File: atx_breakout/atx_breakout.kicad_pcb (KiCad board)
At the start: 2 copper layers, 1 part, among them J1 ATX-24

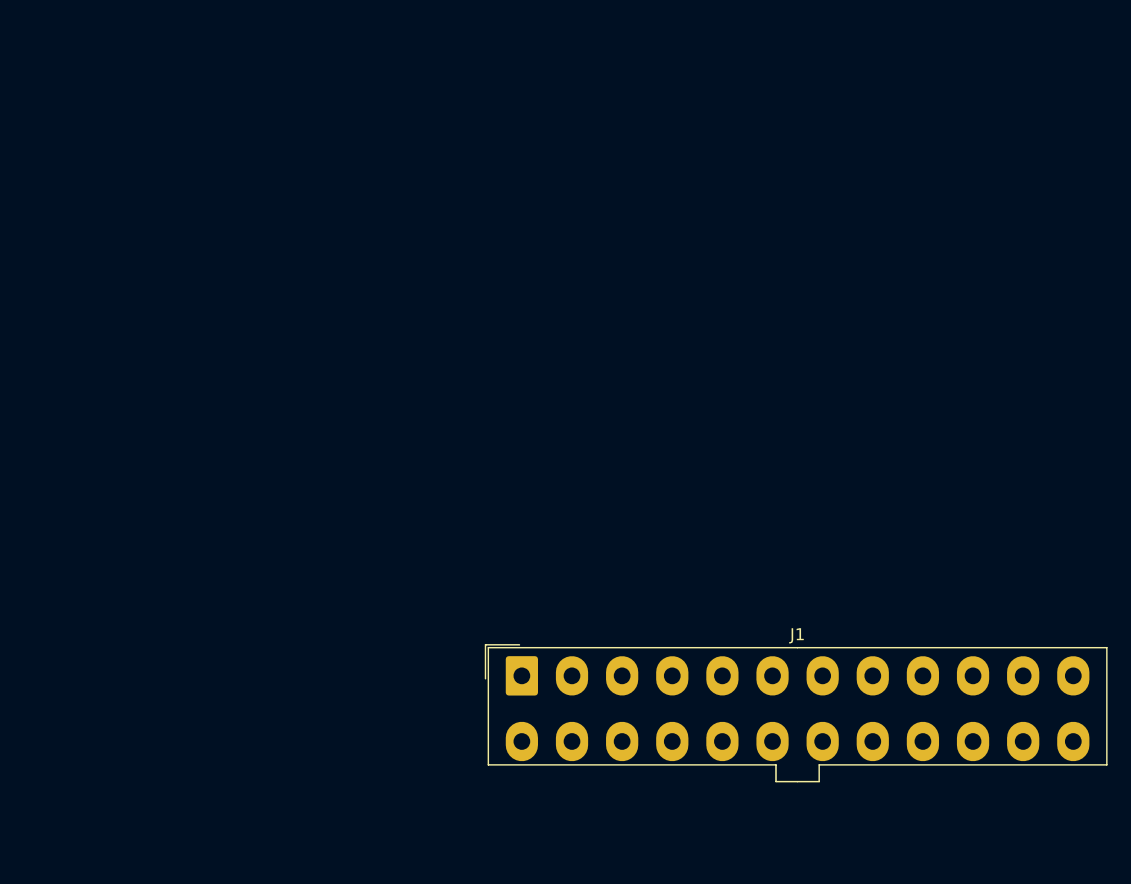
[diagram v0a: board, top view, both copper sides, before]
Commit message: Progress on atx breakout
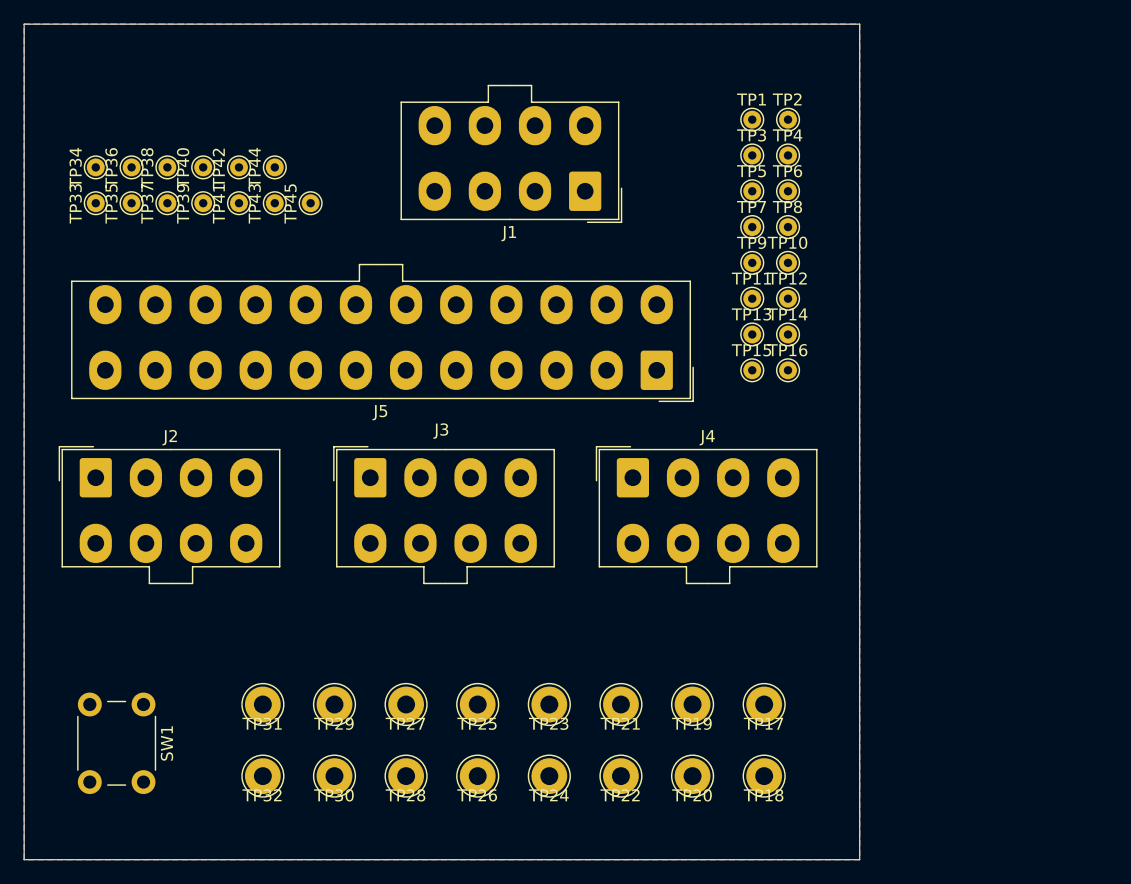
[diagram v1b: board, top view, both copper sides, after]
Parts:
- added J2: Conn_02x04_Top_Bottom, Connector_Molex:Molex_Mini-Fit_Jr_5566-08A_2x04_P4.20mm_Vertical, F.Cu at (6.00, 38.0)
- added J3: Conn_02x04_Top_Bottom, Connector_Molex:Molex_Mini-Fit_Jr_5566-08A_2x04_P4.20mm_Vertical, F.Cu at (29.0, 38.0)
- added J4: Conn_02x04_Top_Bottom, Connector_Molex:Molex_Mini-Fit_Jr_5566-08A_2x04_P4.20mm_Vertical, F.Cu at (51.0, 38.0)
- added J5: ATX-24, Connector_Molex:Molex_Mini-Fit_Jr_5566-24A_2x12_P4.20mm_Vertical, F.Cu at (53.0, 29.0)
- added SW1: SW_SPST, Button_Switch_THT:SW_PUSH_6mm, F.Cu at (10.0, 57.0)
- added TP1: TestPoint, TestPoint:TestPoint_THTPad_D1.5mm_Drill0.7mm, F.Cu at (61.0, 8.00)
- added TP10: TestPoint, TestPoint:TestPoint_THTPad_D1.5mm_Drill0.7mm, F.Cu at (64.0, 20.0)
- added TP11: TestPoint, TestPoint:TestPoint_THTPad_D1.5mm_Drill0.7mm, F.Cu at (61.0, 23.0)
- added TP12: TestPoint, TestPoint:TestPoint_THTPad_D1.5mm_Drill0.7mm, F.Cu at (64.0, 23.0)
- added TP13: TestPoint, TestPoint:TestPoint_THTPad_D1.5mm_Drill0.7mm, F.Cu at (61.0, 26.0)
- added TP14: TestPoint, TestPoint:TestPoint_THTPad_D1.5mm_Drill0.7mm, F.Cu at (64.0, 26.0)
- added TP15: TestPoint, TestPoint:TestPoint_THTPad_D1.5mm_Drill0.7mm, F.Cu at (61.0, 29.0)
- added TP16: TestPoint, TestPoint:TestPoint_THTPad_D1.5mm_Drill0.7mm, F.Cu at (64.0, 29.0)
- added TP17: TestPoint, TestPoint:TestPoint_THTPad_D3.0mm_Drill1.5mm, F.Cu at (62.0, 57.0)
- added TP18: TestPoint, TestPoint:TestPoint_THTPad_D3.0mm_Drill1.5mm, F.Cu at (62.0, 63.0)
- added TP19: TestPoint, TestPoint:TestPoint_THTPad_D3.0mm_Drill1.5mm, F.Cu at (56.0, 57.0)
- added TP2: TestPoint, TestPoint:TestPoint_THTPad_D1.5mm_Drill0.7mm, F.Cu at (64.0, 8.00)
- added TP20: TestPoint, TestPoint:TestPoint_THTPad_D3.0mm_Drill1.5mm, F.Cu at (56.0, 63.0)
- added TP21: TestPoint, TestPoint:TestPoint_THTPad_D3.0mm_Drill1.5mm, F.Cu at (50.0, 57.0)
- added TP22: TestPoint, TestPoint:TestPoint_THTPad_D3.0mm_Drill1.5mm, F.Cu at (50.0, 63.0)
- added TP23: TestPoint, TestPoint:TestPoint_THTPad_D3.0mm_Drill1.5mm, F.Cu at (44.0, 57.0)
- added TP24: TestPoint, TestPoint:TestPoint_THTPad_D3.0mm_Drill1.5mm, F.Cu at (44.0, 63.0)
- added TP25: TestPoint, TestPoint:TestPoint_THTPad_D3.0mm_Drill1.5mm, F.Cu at (38.0, 57.0)
- added TP26: TestPoint, TestPoint:TestPoint_THTPad_D3.0mm_Drill1.5mm, F.Cu at (38.0, 63.0)
- added TP27: TestPoint, TestPoint:TestPoint_THTPad_D3.0mm_Drill1.5mm, F.Cu at (32.0, 57.0)
- added TP28: TestPoint, TestPoint:TestPoint_THTPad_D3.0mm_Drill1.5mm, F.Cu at (32.0, 63.0)
- added TP29: TestPoint, TestPoint:TestPoint_THTPad_D3.0mm_Drill1.5mm, F.Cu at (26.0, 57.0)
- added TP3: TestPoint, TestPoint:TestPoint_THTPad_D1.5mm_Drill0.7mm, F.Cu at (61.0, 11.0)
- added TP30: TestPoint, TestPoint:TestPoint_THTPad_D3.0mm_Drill1.5mm, F.Cu at (26.0, 63.0)
- added TP31: TestPoint, TestPoint:TestPoint_THTPad_D3.0mm_Drill1.5mm, F.Cu at (20.0, 57.0)
- added TP32: TestPoint, TestPoint:TestPoint_THTPad_D3.0mm_Drill1.5mm, F.Cu at (20.0, 63.0)
- added TP33: TestPoint, TestPoint:TestPoint_THTPad_D1.5mm_Drill0.7mm, F.Cu at (6.00, 15.0)
- added TP34: TestPoint, TestPoint:TestPoint_THTPad_D1.5mm_Drill0.7mm, F.Cu at (6.00, 12.0)
- added TP35: TestPoint, TestPoint:TestPoint_THTPad_D1.5mm_Drill0.7mm, F.Cu at (9.00, 15.0)
- added TP36: TestPoint, TestPoint:TestPoint_THTPad_D1.5mm_Drill0.7mm, F.Cu at (9.00, 12.0)
- added TP37: TestPoint, TestPoint:TestPoint_THTPad_D1.5mm_Drill0.7mm, F.Cu at (12.0, 15.0)
- added TP38: TestPoint, TestPoint:TestPoint_THTPad_D1.5mm_Drill0.7mm, F.Cu at (12.0, 12.0)
- added TP39: TestPoint, TestPoint:TestPoint_THTPad_D1.5mm_Drill0.7mm, F.Cu at (15.0, 15.0)
- added TP4: TestPoint, TestPoint:TestPoint_THTPad_D1.5mm_Drill0.7mm, F.Cu at (64.0, 11.0)
- added TP40: TestPoint, TestPoint:TestPoint_THTPad_D1.5mm_Drill0.7mm, F.Cu at (15.0, 12.0)
- added TP41: TestPoint, TestPoint:TestPoint_THTPad_D1.5mm_Drill0.7mm, F.Cu at (18.0, 15.0)
- added TP42: TestPoint, TestPoint:TestPoint_THTPad_D1.5mm_Drill0.7mm, F.Cu at (18.0, 12.0)
- added TP43: TestPoint, TestPoint:TestPoint_THTPad_D1.5mm_Drill0.7mm, F.Cu at (21.0, 15.0)
- added TP44: TestPoint, TestPoint:TestPoint_THTPad_D1.5mm_Drill0.7mm, F.Cu at (21.0, 12.0)
- added TP45: TestPoint, TestPoint:TestPoint_THTPad_D1.5mm_Drill0.7mm, F.Cu at (24.0, 15.0)
- added TP5: TestPoint, TestPoint:TestPoint_THTPad_D1.5mm_Drill0.7mm, F.Cu at (61.0, 14.0)
- added TP6: TestPoint, TestPoint:TestPoint_THTPad_D1.5mm_Drill0.7mm, F.Cu at (64.0, 14.0)
- added TP7: TestPoint, TestPoint:TestPoint_THTPad_D1.5mm_Drill0.7mm, F.Cu at (61.0, 17.0)
- added TP8: TestPoint, TestPoint:TestPoint_THTPad_D1.5mm_Drill0.7mm, F.Cu at (64.0, 17.0)
- added TP9: TestPoint, TestPoint:TestPoint_THTPad_D1.5mm_Drill0.7mm, F.Cu at (61.0, 20.0)
- J1: value ATX-24 -> Conn_02x04_Top_Bottom; footprint Connector_Molex:Molex_Mini-Fit_Jr_5566-24A_2x12_P4.20mm_Vertical -> Connector_Molex:Molex_Mini-Fit_Jr_5566-08A_2x04_P4.20mm_Vertical
- moved J1 40.9 mm to (47.0, 14.0), turned to 180 degrees
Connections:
- J1 pad 1: Net-(J1-+3.3V-Pad1) -> GND
- J1 pad 2: Net-(J1-+3.3V-Pad1) -> GND
- J1 pad 3: Net-(J1-GND-Pad15) -> GND
- J1 pad 4: Net-(J1-+5V-Pad21) -> GND
- J1 pad 5: Net-(J1-GND-Pad15) -> +12V
- J1 pad 6: Net-(J1-+5V-Pad21) -> +12V
- J1 pad 7: Net-(J1-GND-Pad15) -> +12V
- J1 pad 8: unconnected-(J1-PWR_OK-Pad8) -> +12V
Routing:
- added copper zone on F.Cu, net +12V
- added copper zone on B.Cu, net GND
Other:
- board outline added: 70 x 70 mm
- rule pad_to_mask_clearance: 0 -> 0.038

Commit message: Progress on atx breakout
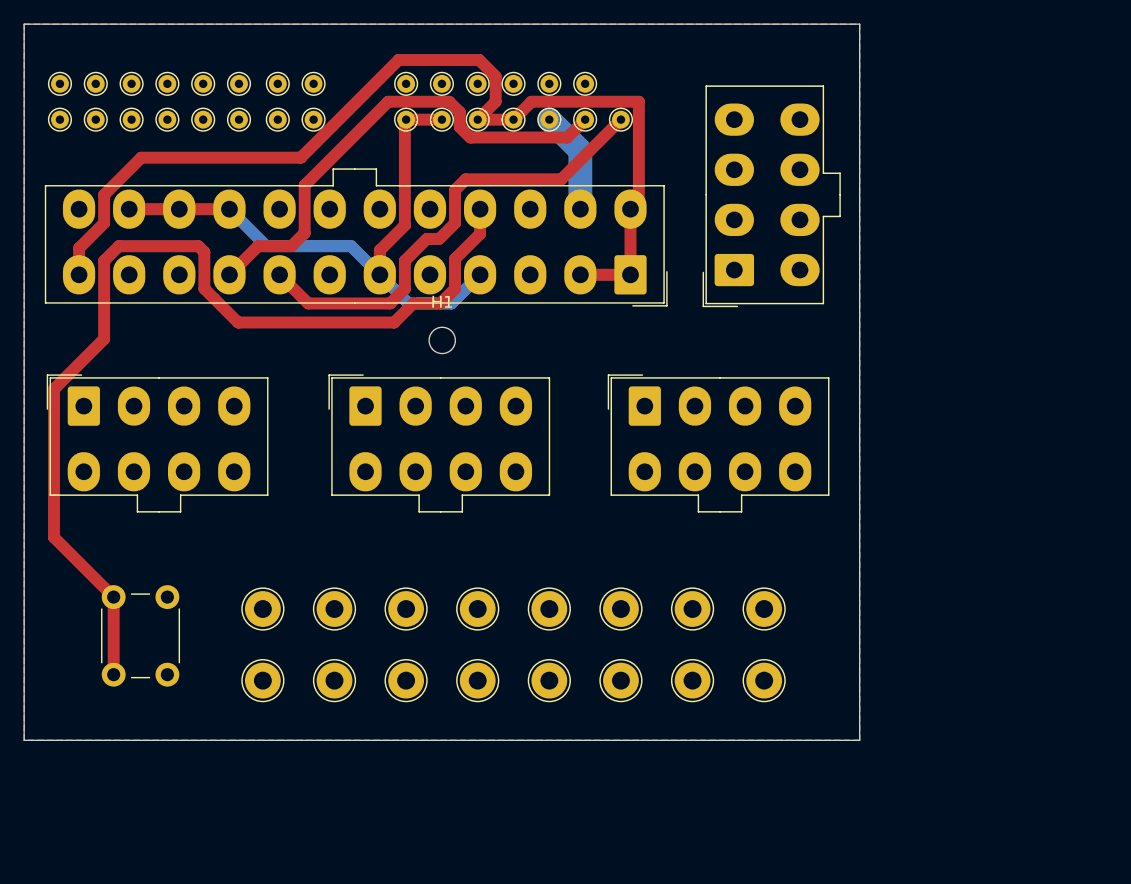
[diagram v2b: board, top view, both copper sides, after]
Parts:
- added H1: MountingHole, MountingHole:MountingHole_2.2mm_M2, F.Cu at (35.0, 26.5)
- moved TP2 61.1 mm to (3.00, 5.00), turned to 90 degrees
- moved TP4 58.3 mm to (6.00, 5.00), turned to 90 degrees
- moved TP1 58.0 mm to (3.00, 8.00), turned to 90 degrees
- moved TP6 55.7 mm to (9.00, 5.00), turned to 90 degrees
- moved TP3 55.1 mm to (6.00, 8.00), turned to 90 degrees
- moved TP8 53.4 mm to (12.0, 5.00), turned to 90 degrees
- moved TP5 52.3 mm to (9.00, 8.00), turned to 90 degrees
- moved TP10 51.2 mm to (15.0, 5.00), turned to 90 degrees
- moved TP7 49.8 mm to (12.0, 8.00), turned to 90 degrees
- moved TP12 49.4 mm to (18.0, 5.00), turned to 90 degrees
- moved TP14 47.6 mm to (21.2, 5.00), turned to 90 degrees
- moved TP9 47.5 mm to (15.0, 8.00), turned to 90 degrees
- moved TP16 46.4 mm to (24.2, 5.00), turned to 90 degrees
- moved TP11 45.5 mm to (18.0, 8.00), turned to 90 degrees
- moved TP13 43.6 mm to (21.2, 8.00), turned to 90 degrees
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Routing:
- net +3.3V: track 0.00 -> 83.0 mm
- net Net-(J5-PS_ON#): track 0.00 -> 81.6 mm
- net +5V: track 0.00 -> 50.6 mm
- net VBUS: track 0.00 -> 40.7 mm
- net /PWR_OK: track 0.00 -> 39.0 mm
- net -12V: track 0.00 -> 8.58 mm
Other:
- board size 70 x 70 mm -> 70 x 60 mm

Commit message: Finished atx breakout
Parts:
- removed SW1: SW_SPST, Button_Switch_THT:SW_PUSH_6mm
- added U1: SW_DPDT_PS-70N, misc:SW_DPDT_PS-70N, F.Cu at (9.00, 51.0)
- J1, J2, J3, J4: footprint Connector_Molex:Molex_Mini-Fit_Jr_5566-08A_2x04_P4.20mm_Vertical -> misc:Molex_Mini-Fit_Jr_5566-08A_2x04_P4.20mm_XY_Vertical
- J5: footprint Connector_Molex:Molex_Mini-Fit_Jr_5566-24A_2x12_P4.20mm_Vertical -> misc:Molex_Mini-Fit_Jr_5566-24A_2x12_P4.20mm_XY_Vertical
- moved J3 1.17 mm to (28.0, 33.0)
- moved J2 1.00 mm to (5.00, 33.0)
- moved J4 1.00 mm to (52.0, 33.0)
- moved J1 0.78 mm to (59.0, 20.0)
- moved H1 0.50 mm to (35.0, 27.0)
- moved TP13 0.25 mm to (21.0, 8.00)
- moved TP14 0.25 mm to (21.0, 5.00)
- moved TP15 0.25 mm to (24.0, 8.00)
- moved TP16 0.25 mm to (24.0, 5.00)
- moved J5 0.20 mm to (51.0, 21.0)
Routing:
- net Net-(J5-PS_ON#): track 81.6 -> 64.4 mm
- net /PWR_OK: track 39.0 -> 55.5 mm
- net +3.3V: track 83.0 -> 67.1 mm
- net VBUS: track 40.7 -> 56.1 mm
- net +5V: track 50.6 -> 56.2 mm
- net -12V: track 8.58 -> 9.96 mm

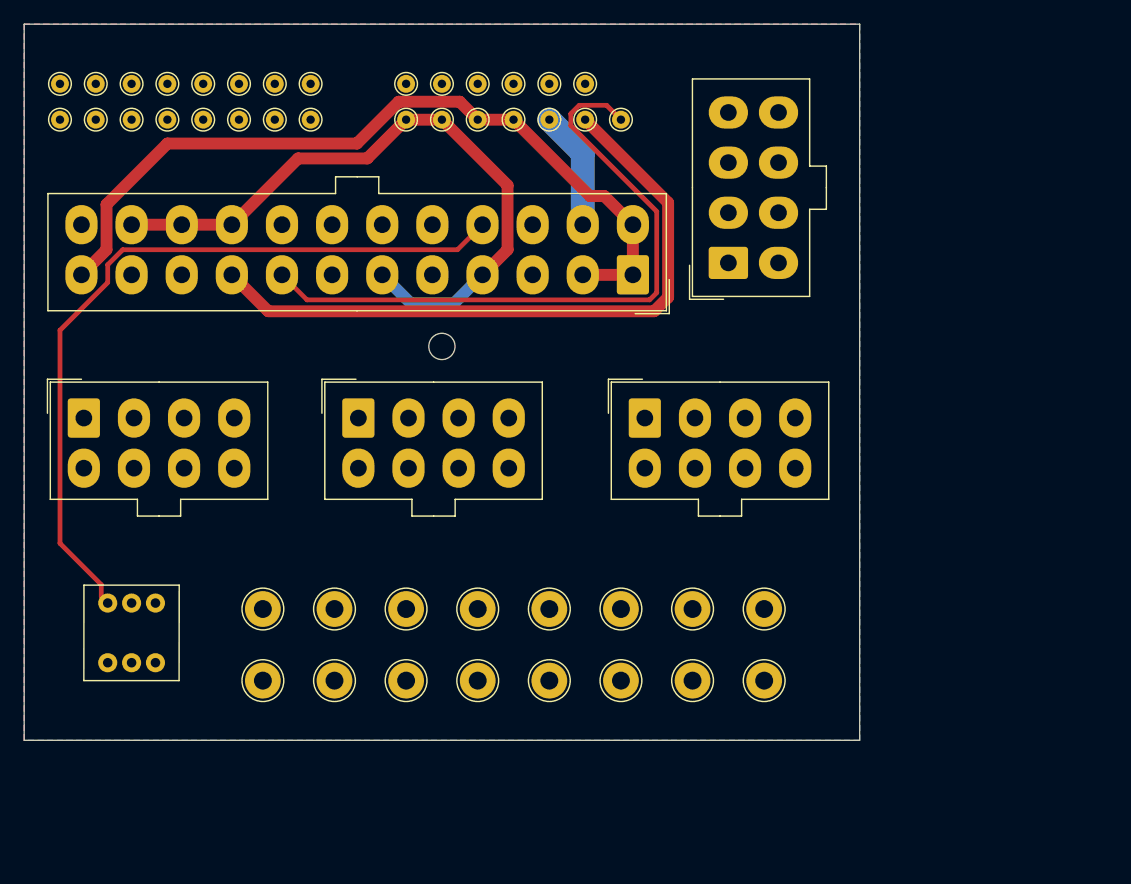
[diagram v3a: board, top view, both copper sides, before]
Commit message: Add atx gerbers
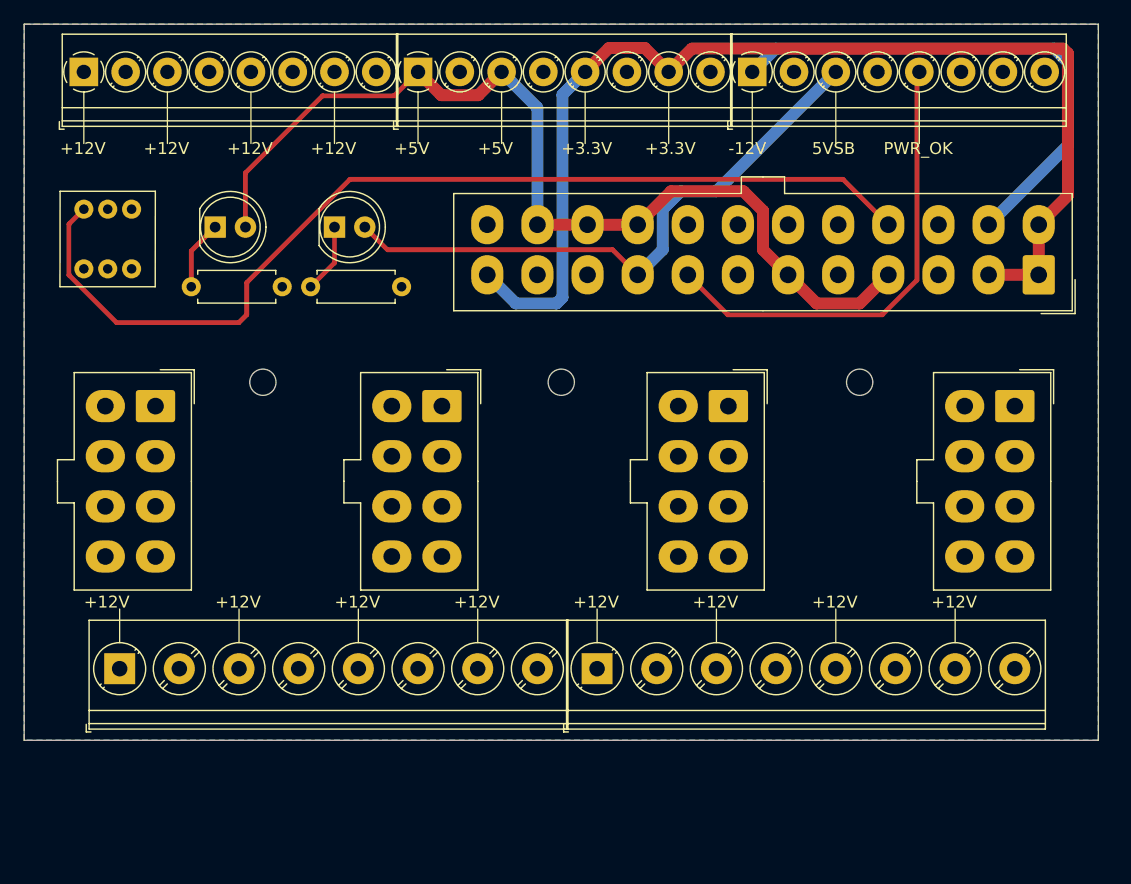
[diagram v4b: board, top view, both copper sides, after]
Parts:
- removed TP1, TP10, TP11, TP12, TP13, TP14, TP15, TP16, TP2, TP3, TP33, TP34, TP35, TP36, TP37, TP38, TP39, TP4, TP40, TP41, TP42, TP43, TP44, TP45, TP5, TP6, TP7, TP8, TP9: TestPoint, TestPoint:TestPoint_THTPad_D1.5mm_Drill0.7mm
- removed TP17, TP18, TP19, TP20, TP21, TP22, TP23, TP24, TP25, TP26, TP27, TP28, TP29, TP30, TP31, TP32: TestPoint, TestPoint:TestPoint_THTPad_D3.0mm_Drill1.5mm
- added D1: LED, LED_THT:LED_D5.0mm, F.Cu at (26.0, 17.0)
- added D2: LED, LED_THT:LED_D5.0mm, F.Cu at (16.0, 17.0)
- added H2: MountingHole, MountingHole:MountingHole_2.2mm_M2, F.Cu at (20.0, 30.0)
- added H3: MountingHole, MountingHole:MountingHole_2.2mm_M2, F.Cu at (70.0, 30.0)
- added J10: Screw_Terminal_01x08, TerminalBlock_Phoenix:TerminalBlock_Phoenix_PT-1,5-8-5.0-H_1x08_P5.00mm_Horizontal, F.Cu at (48.0, 54.0)
- added J6: Screw_Terminal_01x08, TerminalBlock_Phoenix:TerminalBlock_Phoenix_PT-1,5-8-3.5-H_1x08_P3.50mm_Horizontal, F.Cu at (5.00, 4.00)
- added J7: Screw_Terminal_01x08, TerminalBlock_Phoenix:TerminalBlock_Phoenix_PT-1,5-8-3.5-H_1x08_P3.50mm_Horizontal, F.Cu at (33.0, 4.00)
- added J8: Screw_Terminal_01x08, TerminalBlock_Phoenix:TerminalBlock_Phoenix_PT-1,5-8-3.5-H_1x08_P3.50mm_Horizontal, F.Cu at (61.0, 4.00)
- added J9: Screw_Terminal_01x08, TerminalBlock_Phoenix:TerminalBlock_Phoenix_PT-1,5-8-5.0-H_1x08_P5.00mm_Horizontal, F.Cu at (8.00, 54.0)
- added R1: R, Resistor_THT:R_Axial_DIN0207_L6.3mm_D2.5mm_P7.62mm_Horizontal, F.Cu at (24.0, 22.0)
- added R2: R, Resistor_THT:R_Axial_DIN0207_L6.3mm_D2.5mm_P7.62mm_Horizontal, F.Cu at (14.0, 22.0)
- moved J1 49.5 mm to (11.0, 32.0), turned to -90 degrees
- moved J5 34.0 mm to (85.0, 21.0)
- moved U1 33.1 mm to (7.00, 18.0)
- moved J3 31.0 mm to (59.0, 32.0), turned to -90 degrees
- moved J4 31.0 mm to (83.0, 32.0), turned to -90 degrees
- moved J2 30.0 mm to (35.0, 32.0), turned to -90 degrees
- moved H1 10.4 mm to (45.0, 30.0)
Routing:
- net -12V: track 9.96 -> 44.1 mm
- net +3.3V: track 67.1 -> 94.8 mm
- net +5V: track 56.2 -> 82.5 mm
- net Net-(J5-PS_ON#): track 64.4 -> 84.5 mm
- net /PWR_OK: track 55.5 -> 39.3 mm
- net VBUS: track 56.1 -> 50.2 mm
- net Net-(D2-K): track 0.00 -> 5.83 mm
- net Net-(D1-K): track 0.00 -> 5.83 mm
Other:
- board size 70 x 60 mm -> 90 x 60 mm
- board text added: "+12V"
- board text added: "+3.3V"
- board text added: "+5V"
- board text added: "-12V"
- board text added: "5VSB"
- board text added: "PWR_OK"

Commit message: Fix bugs (gerbers not updated)
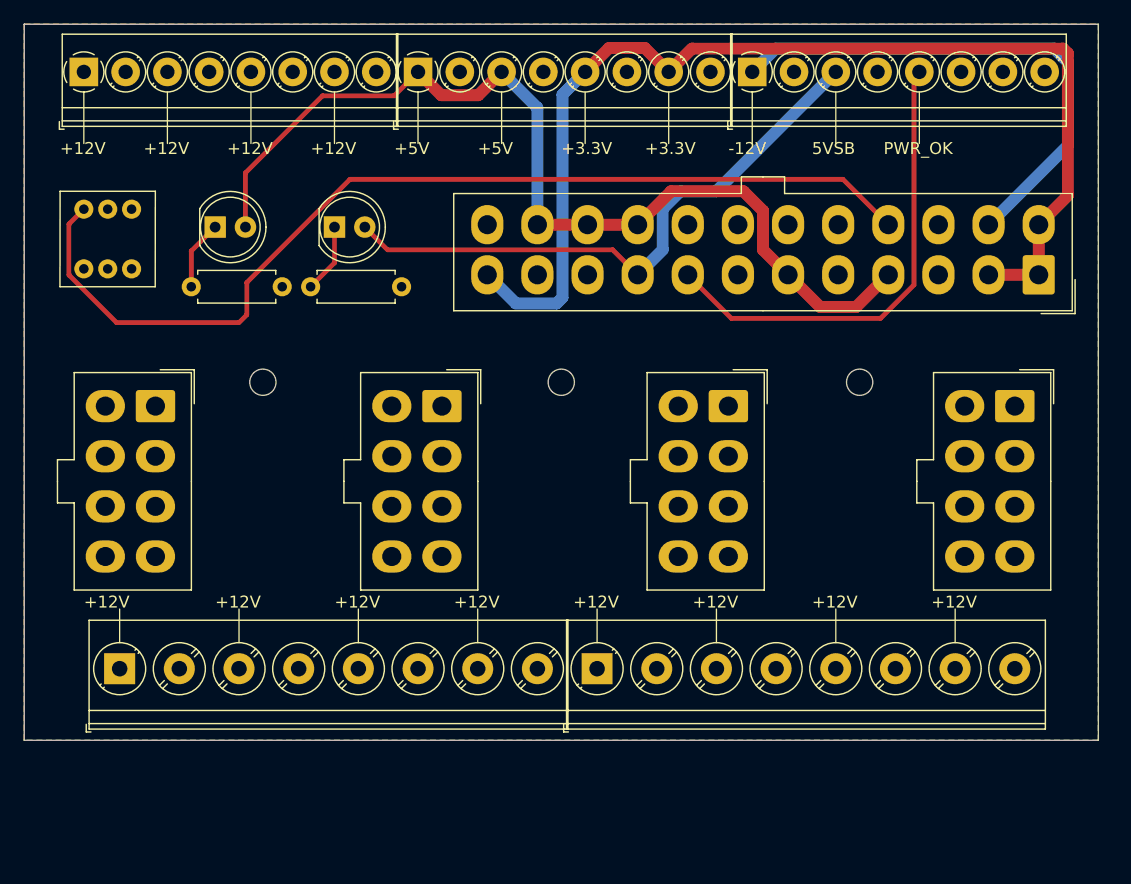
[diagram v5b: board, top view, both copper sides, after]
